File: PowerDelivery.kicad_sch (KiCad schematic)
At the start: 0 parts

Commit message: update readme, WIP on PD
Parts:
- added C1, C3, C6: 1u, symbol Device:C_Small
- added C2, C4, C5: 100n, symbol Device:C_Small
- added U1: CYPD3177_24x, Cake_USB:CYPD3177_24LQx_QFN-24_EP_4x4_Pitch0.5mm, symbol Cake_USB:CYPD3177_24x
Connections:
- new net: C3.1, C4.1, C5.1, U1.23 (VDDD)
- new net: C6.1, U1.24 (VCCD)
- new net GND: C1.2, C2.2, C3.2, C4.2, C5.2, C6.2, U1.19 (GND), U1.22 (VSS), U1.25 (EPAD)
- new net USB_UFP_CC1: U1.15 (CC1)
- new net USB_UFP_CC2: U1.14 (CC2)
- new net USB_UFP_VBUS: C1.1, C2.1, U1.18 (VBUS_IN)

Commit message: more WIP on power delivery
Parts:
- removed C4, C5: 100n, symbol Device:C_Small
- added C7: 1u, symbol Device:C_Small
- added C8, C9: 100n, symbol Device:C_Small
- added D1: RED, symbol Device:LED
- added D2: D_Zener, symbol Device:D_Zener
- added Q1, Q2: SI3421DV, Package_TO_SOT_SMD:SOT-23-6, symbol catSink:SI3421DV
- added R1, R3, R4: 5k1, symbol Device:R
- added R2, R5, R7: 10k, symbol Device:R
- added R6: 1k, symbol Device:R
- added R8: 50k, symbol Device:R
- C1: value 1u -> 3u3
- C2: value 100n -> 1u
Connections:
- net GND: now also C7.2, C8.2, C9.2, R2.2, R3.2, R4.2, R5.2; no longer C2.2, C3.2
- net at U1.1 (VBUS_MIN): now also R3.1
- net +20V: now reaches U1.11 (VDC_OUT)
- net +20V: now also C3.1, Q2.1 (D), Q2.2 (D1), Q2.5 (D2), Q2.6 (D3)
- net USB_PD_VDDD_3V3: now reaches U1.2 (VBUS_MAX)
- net USB_PD_VDDD_3V3: now also U1.23 (VDDD), C7.1, C8.1, C9.1, R1.1
- net at U1.3 (VBUS_FET_EN): now also R6.2
- net at U1.5 (ISNK_COARSE): now also R1.2, R2.1
- net at U1.6 (ISNK_FINE): now also R4.1
- net FAULT: now reaches U1.9 (FAULT)
- net FAULT: now also D1.2 (A)
- net USB_UFP_VBUS renamed VBUS
- net VBUS: now also Q1.1 (D), Q1.2 (D1), Q1.5 (D2), Q1.6 (D3), R7.1
- new net: C2.2, C3.2, D2.2 (A), Q1.3 (G), Q2.3 (G), R6.1, R7.2, R8.2
- new net: D2.1 (K), Q1.4 (S), Q2.4 (S), R8.1
- new net: D1.1 (K), R5.1
- no-connect marks 0 -> 1
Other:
- note added: "For a current setting of 4A, resistor ratio should be 4/6."
- moved on the sheet: C1, C6

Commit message: finish PD controller schematic
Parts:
- added R10, R9: 10k, symbol Device:R
- R2: value 10k -> 5k1
- R3: value 5k1 -> 10k
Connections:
- net GND: no longer R3.2
- net USB_PD_VDDD_3V3: now also R3.1, U1.1 (VBUS_MIN), R10.1, R9.1
- net USB_UFP_FLIP: now reaches U1.10 (FLIP)
- net at U1.12 (HPI_SDA): now also R3.2
- net at U1.13 (HPI_SCL): now also R9.2
- net at U1.7 (HPI_INT): now also R10.2
- no-connect marks 1 -> 2
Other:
- note added: "FAULT is driven high if voltage or current requested cannot be met, or if VBUS_IN is >20% off."
- note added: "For a current setting of 3A, resistor ratio should be 3/6."
- note removed: "For a current setting of 4A, resistor ratio should be 4/6."
- moved on the sheet: D1, R1, R2, R4, R5

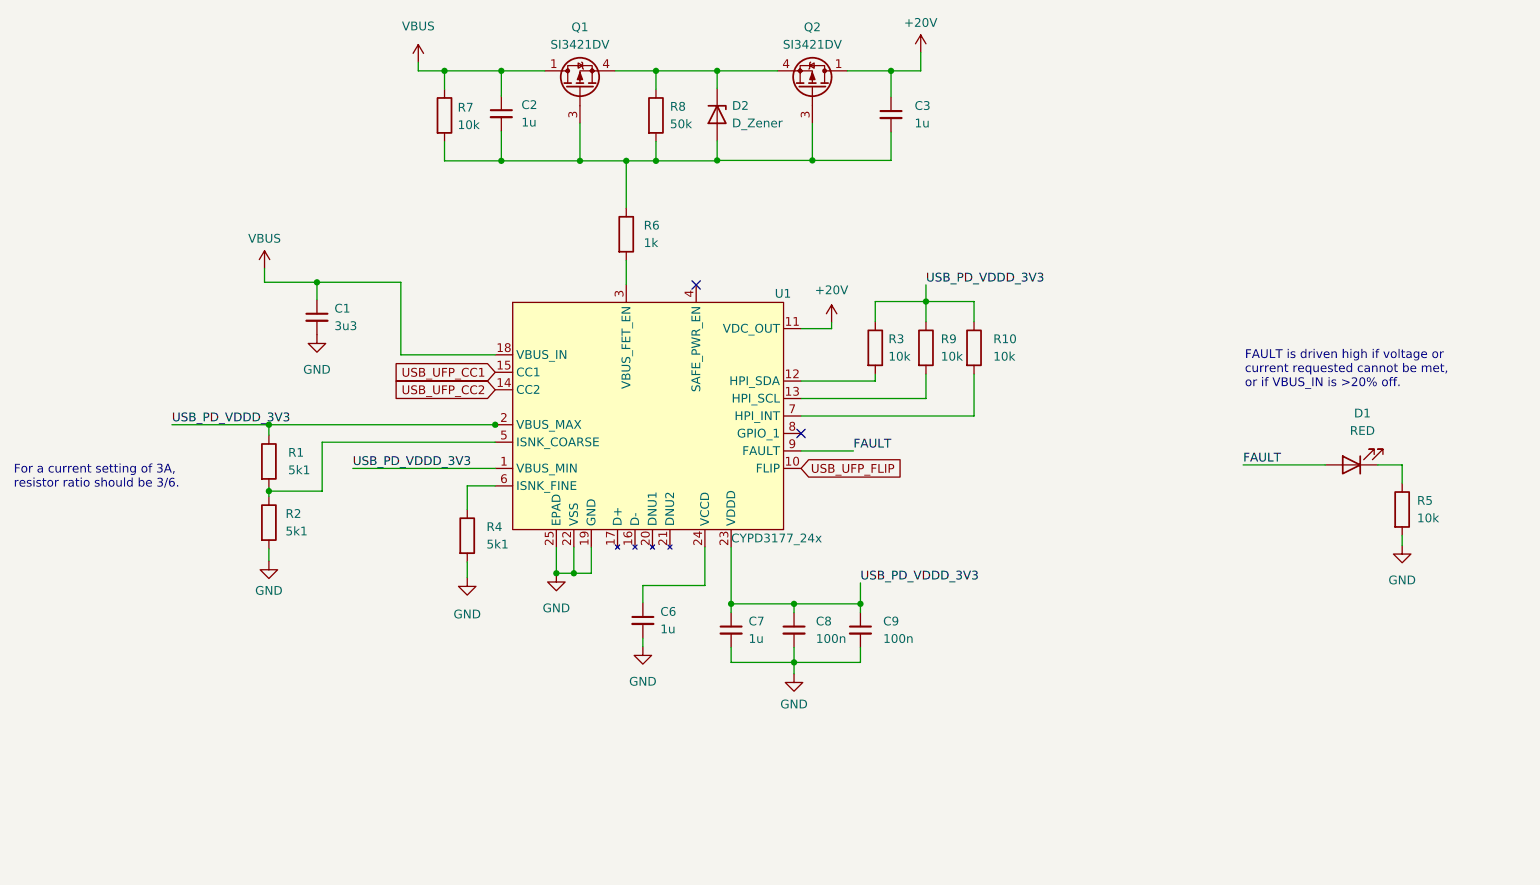
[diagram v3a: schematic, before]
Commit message: update grid spacing
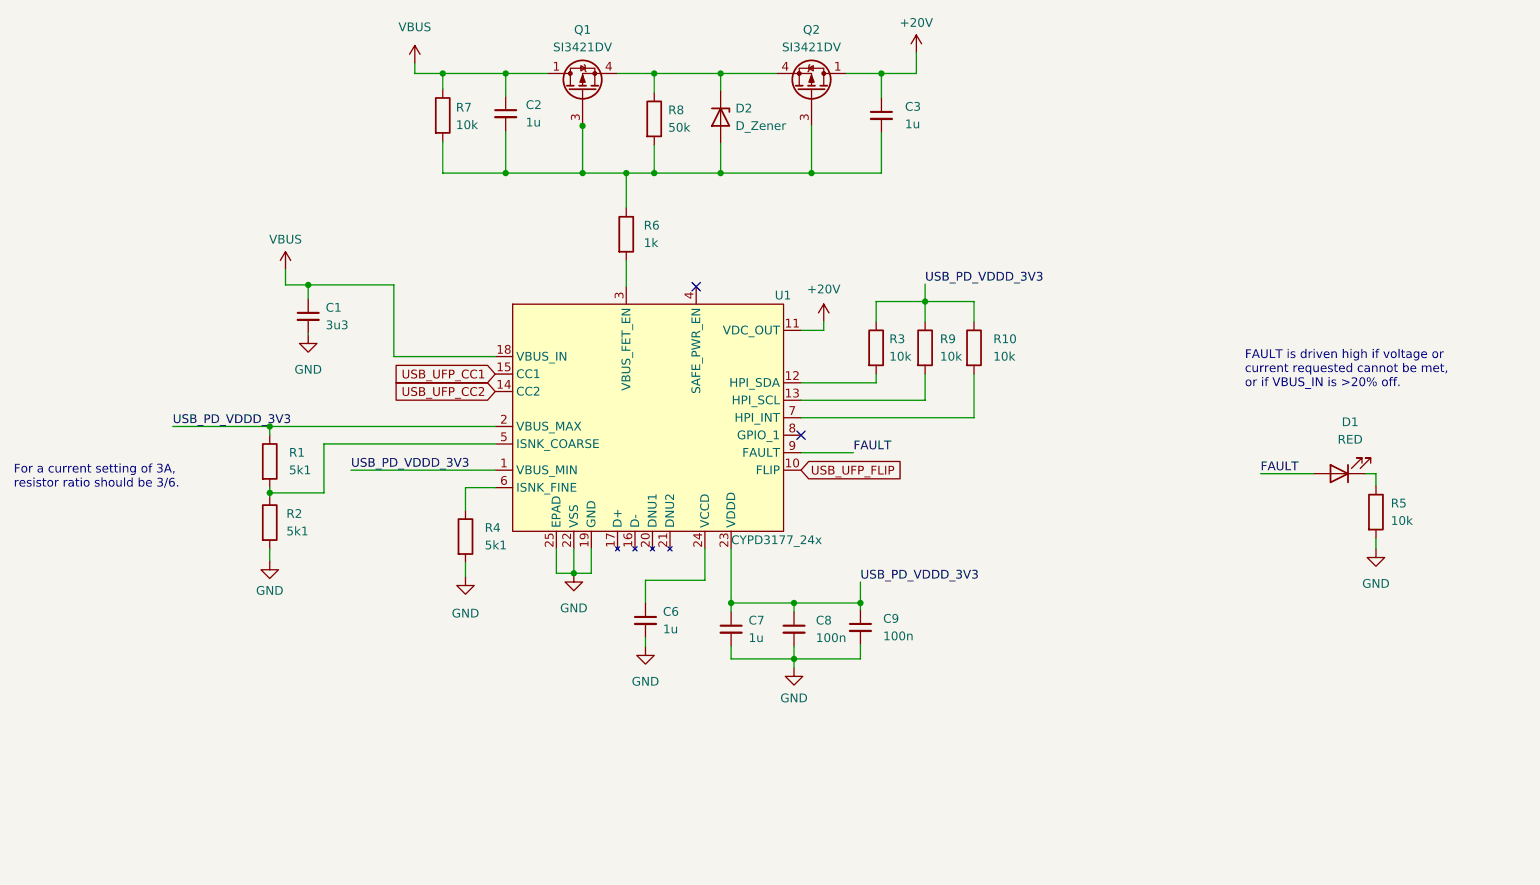
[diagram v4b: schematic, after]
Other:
- moved on the sheet: C1, C2, C3, D1, D2, Q1, R5, R8

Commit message: fix warnings
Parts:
- added J1: Screw_Terminal_01x02, symbol Connector:Screw_Terminal_01x02
- renumbered C2 to C1, C3 to C2, C1 to C3, C6 to C4, C9 to C5, C7 to C6, C8 to C7, D2 to D1, D1 to D2, R7 to R1, R5 to R10, R8 to R2, R6 to R3, R3 to R4, R9 to R5, R10 to R6, R1 to R7, R2 to R8, R4 to R9
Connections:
- net +20V: now also J1.1 (Pin_1)
- net GND: now also J1.2 (Pin_2)

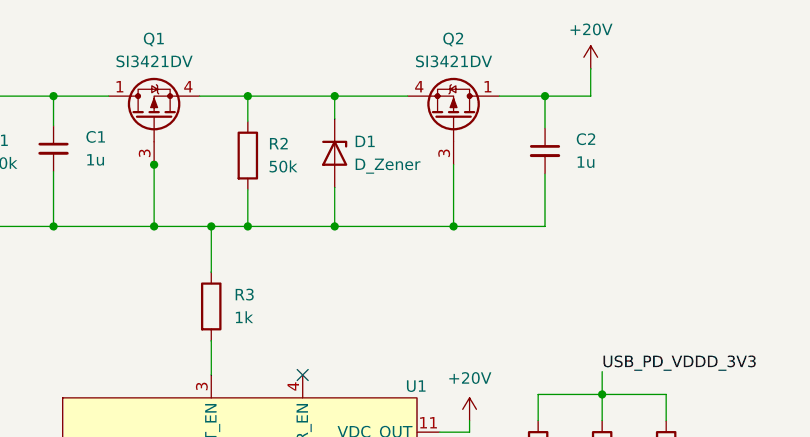
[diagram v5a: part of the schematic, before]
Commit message: paste kicad symbols and libs directly in here
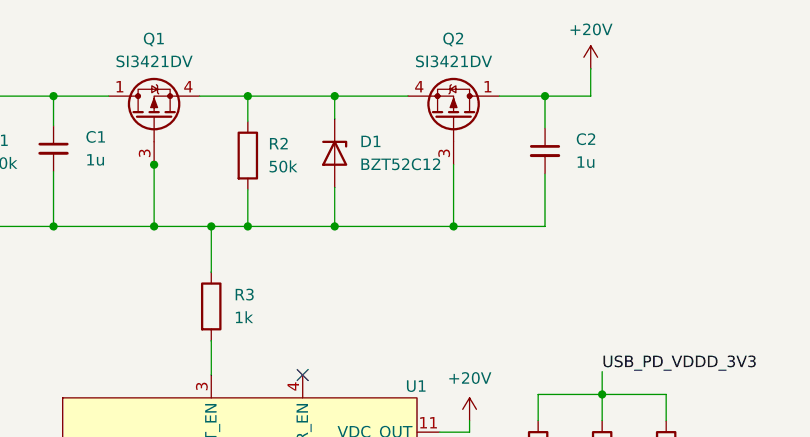
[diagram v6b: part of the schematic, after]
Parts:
- C1, C2, C3, C4, C5, C6, C7: footprint (none) -> Capacitor_SMD:C_0603_1608Metric
- D1: value D_Zener -> BZT52C12
- R1, R10, R2, R3, R4, R5, R6, R7, R8, R9: footprint (none) -> Resistor_SMD:R_0603_1608Metric
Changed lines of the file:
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@@
       (effects (font (size 1.27 1.27)) (justify left))
     )
-    (property "Footprint" "" (at 90.424 58.928 0)
+    (property "Footprint" "Capacitor_SMD:C_0603_1608Metric" (at 90.424 58.928 0)
       (effects (font (size 1.27 1.27)) hide)
     )
@@
       (effects (font (size 1.27 1.27)) (justify left))
     )
-    (property "Footprint" "" (at 54.356 109.474 90)
+    (property "Footprint" "Resistor_SMD:R_0603_1608Metric" (at 54.356 109.474 90)
       (effects (font (size 1.27 1.27)) hide)
     )
@@
       (effects (font (size 1.27 1.27)) (justify left))
     )
-    (property "Footprint" "" (at 79.502 59.182 90)
+    (property "Footprint" "Resistor_SMD:R_0603_1608Metric" (at 79.502 59.182 90)
       (effects (font (size 1.27 1.27)) hide)
     )
@@
       (effects (font (size 1.27 1.27)) (justify left))
     )
-    (property "Footprint" "" (at 141.986 133.604 0)
+    (property "Footprint" "Capacitor_SMD:C_0603_1608Metric" (at 141.986 133.604 0)
       (effects (font (size 1.27 1.27)) hide)
     )
@@
       (effects (font (size 1.27 1.27)) (justify left))
     )
-    (property "Footprint" "" (at 106.172 76.454 90)
+    (property "Footprint" "Resistor_SMD:R_0603_1608Metric" (at 106.172 76.454 90)
       (effects (font (size 1.27 1.27)) hide)
     )
@@
       (effects (font (size 1.27 1.27)) (justify left))
     )
-    (property "Footprint" "" (at 215.138 116.84 90)
+    (property "Footprint" "Resistor_SMD:R_0603_1608Metric" (at 215.138 116.84 90)
       (effects (font (size 1.27 1.27)) hide)
     )
@@
       (effects (font (size 1.27 1.27)) (justify left))
     )
-    (property "Footprint" "" (at 82.804 120.396 90)
+    (property "Footprint" "Resistor_SMD:R_0603_1608Metric" (at 82.804 120.396 90)
       (effects (font (size 1.27 1.27)) hide)
     )
@@
       (effects (font (size 1.27 1.27)) (justify left))
     )
-    (property "Footprint" "" (at 61.722 88.392 0)
+    (property "Footprint" "Capacitor_SMD:C_0603_1608Metric" (at 61.722 88.392 0)
       (effects (font (size 1.27 1.27)) hide)
     )
@@
       (effects (font (size 1.27 1.27)) (justify left))
     )
-    (property "Footprint" "" (at 110.744 132.588 0)
+    (property "Footprint" "Capacitor_SMD:C_0603_1608Metric" (at 110.744 132.588 0)
       (effects (font (size 1.27 1.27)) hide)
     )
@@
       (effects (font (size 1.27 1.27)) (justify left))
     )
-    (property "Footprint" "" (at 110.236 59.69 90)
+    (property "Footprint" "Resistor_SMD:R_0603_1608Metric" (at 110.236 59.69 90)
       (effects (font (size 1.27 1.27)) hide)
     )
@@
       (effects (font (size 1.27 1.27)) (justify left))
     )
-    (property "Footprint" "" (at 145.034 59.182 0)
+    (property "Footprint" "Capacitor_SMD:C_0603_1608Metric" (at 145.034 59.182 0)
       (effects (font (size 1.27 1.27)) hide)
     )
@@
       (effects (font (size 1.27 1.27)) (justify left))
     )
-    (property "Footprint" "" (at 123.19 133.858 0)
+    (property "Footprint" "Capacitor_SMD:C_0603_1608Metric" (at 123.19 133.858 0)
       (effects (font (size 1.27 1.27)) hide)
     )
@@
       (effects (font (size 1.27 1.27)) (justify left))
     )
-    (property "Footprint" "" (at 149.606 92.964 90)
+    (property "Footprint" "Resistor_SMD:R_0603_1608Metric" (at 149.606 92.964 90)
       (effects (font (size 1.27 1.27)) hide)
     )
@@
       (effects (font (size 1.27 1.27)) (justify left))
     )
-    (property "Footprint" "" (at 156.718 92.964 90)
+    (property "Footprint" "Resistor_SMD:R_0603_1608Metric" (at 156.718 92.964 90)
       (effects (font (size 1.27 1.27)) hide)
     )
@@
   (symbol (lib_id "Device:D_Zener") (at 121.666 59.436 270) (unit 1)
     (in_bom yes) (on_board yes) (dnp no) (fields_autoplaced)
-    (property "Reference" "D1" (at 123.825 58.166 90)
-      (effects (font (size 1.27 1.27)) (justify left))
-    )
-    (property "Value" "D_Zener" (at 123.825 60.706 90)
+    (property "Reference" "D1" (at 124.46 58.166 90)
+      (effects (font (size 1.27 1.27)) (justify left))
+    )
+    (property "Value" "BZT52C12" (at 124.46 60.706 90)
       (effects (font (size 1.27 1.27)) (justify left))
     )
@@
       (effects (font (size 1.27 1.27)) (justify left))
     )
-    (property "Footprint" "" (at 54.356 118.364 90)
+    (property "Footprint" "Resistor_SMD:R_0603_1608Metric" (at 54.356 118.364 90)
       (effects (font (size 1.27 1.27)) hide)
     )
@@
       (effects (font (size 1.27 1.27)) (justify left))
     )
-    (property "Footprint" "" (at 132.334 133.858 0)
+    (property "Footprint" "Capacitor_SMD:C_0603_1608Metric" (at 132.334 133.858 0)
       (effects (font (size 1.27 1.27)) hide)
     )
@@
       (effects (font (size 1.27 1.27)) (justify left))
     )
-    (property "Footprint" "" (at 142.494 92.964 90)
-      (effects (font (size 1.27 1.27)) hide)
-    )
+    (property "Footprint" "Resistor_SMD:R_0603_1608Metric" (at 142.494 92.964 90)
+      (effects (font (size 1.27 1.27)) hide)
+    )

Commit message: start layout of usb PD
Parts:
- removed C1, C2, C4, C6: 1u, Capacitor_SMD:C_0603_1608Metric, symbol Device:C_Small
- removed C3: 3u3, Capacitor_SMD:C_0603_1608Metric, symbol Device:C_Small
- removed C5, C7: 100n, Capacitor_SMD:C_0603_1608Metric, symbol Device:C_Small
- removed D1: BZT52C12, symbol Device:D_Zener
- removed D2: RED, symbol Device:LED
- removed J1: Screw_Terminal_01x02, symbol Connector:Screw_Terminal_01x02
- removed Q1, Q2: SI3421DV, Package_TO_SOT_SMD:SOT-23-6, symbol catSink:SI3421DV
- removed R1, R10, R4, R5, R6: 10k, Resistor_SMD:R_0603_1608Metric, symbol Device:R
- removed R2: 50k, Resistor_SMD:R_0603_1608Metric, symbol Device:R
- removed R3: 1k, Resistor_SMD:R_0603_1608Metric, symbol Device:R
- removed R7, R8, R9: 5k1, Resistor_SMD:R_0603_1608Metric, symbol Device:R
- removed U1: CYPD3177_24x, Cake_USB:CYPD3177_24LQx_QFN-24_EP_4x4_Pitch0.5mm, symbol Cake_USB:CYPD3177_24x
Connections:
- no-connect marks 2 -> 0
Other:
- note removed: "FAULT is driven high if voltage or current requested cannot be met, or if VBUS_IN is >20% off."
- note removed: "For a current setting of 3A, resistor ratio should be 3/6."
